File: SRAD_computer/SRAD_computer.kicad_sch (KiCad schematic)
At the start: 66 parts, among them J1 Terminal_3, J2 Conn_01x02, J3 UJ20-C-H-G-SMT-1-P16-TR, J4 Terminal_2, J5 Connector_3_Pol, J6 Micro_SD_Card, Q1 MMBT5551L, Q3 FDN340P, U1 NCP1117-3.3_SOT223, U2 W25Q128JVS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

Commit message: SD layout
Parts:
- added C18: 10u, TCLib:C_0805, symbol TCLib:C
- added R13: R, TCLib:R_0805, symbol TCLib:R
- added R14, R15: 10k, TCLib:R_0805, symbol TCLib:R
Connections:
- net +3V3: now also J6.4 (VDD), C18.1, R14.1, R15.1
- net GND: now also J6.6 (VSS), C18.2, R13.2
- net SD_CLK: now also U3.31 (GPIO20), R13.1; no longer U3.32 (GPIO21)
- net SD_CMD: now also U3.32 (GPIO21); no longer U3.34 (GPIO22)
- net SD_DAT1: now also U3.37 (GPIO25), R15.2; no longer U3.29 (GPIO18)
- net SD_DAT2: now also U3.35 (GPIO23), R14.2; no longer U3.37 (GPIO25)
- net SD_DAT3: now also U3.34 (GPIO22); no longer U3.35 (GPIO23)
- removed net SD_VSS: J6.6 (VSS), U3.31 (GPIO20)
- new net GPIO18: U3.29 (GPIO18)
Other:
- moved on the sheet: C10, C11, C12, C13, C14, C15, C16, C17, C6, C7, C8, C9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

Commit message: USB footprint changed & reboot sw added
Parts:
- removed J3: UJ20-C-H-G-SMT-1-P16-TR, my_lib:USB-C-samesky, symbol UJ20-C-H-G-SMT-1-P16-TR:UJ20-C-H-G-SMT-1-P16-TR
- added J7: UJ20-C-H-G-SMT-6-P16-TR, my_lib:SAMESKY_UJ20-C-H-G-SMT-6-P16-TR, symbol Rocketry_FC:UJ20-C-H-G-SMT-6-P16-TR
- added R16: 10k, TCLib:R_0805, symbol TCLib:R
- added S2: PTS810SJK250SMTR_LFS, PTS810SJK250SMTRLFS, symbol Rocketry_FC:PTS810SJK250SMTR_LFS
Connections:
- net +3V3: now also R16.1
- net GND: now also J7.A1 (GND), J7.A12 (GND__1), J7.B1 (GND__2), J7.B12 (GND__3), J7.SH1 (SHIELD), J7.SH2 (SHIELD__1), J7.SH3 (SHIELD__2), J7.SH4 (SHIELD__3), J7.SH5 (SHIELD__4), J7.SH6 (SHIELD__5), S2.3 (COM_1), S2.4 (COM_2)
- net RUN: now also R16.2, S2.1 (NO_1), S2.2 (NO_2)
- net USB_D+: now also J7.A6 (DP1), J7.B6 (DP2)
- net USB_D-: now also J7.A7 (DN1), J7.B7 (DN2)
- net VBUS: now also J7.A4 (VBUS), J7.A9 (VBUS__1), J7.B4 (VBUS__2), J7.B9 (VBUS__3)
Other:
- moved on the sheet: C2, C3, R12, R5, S1, Y1

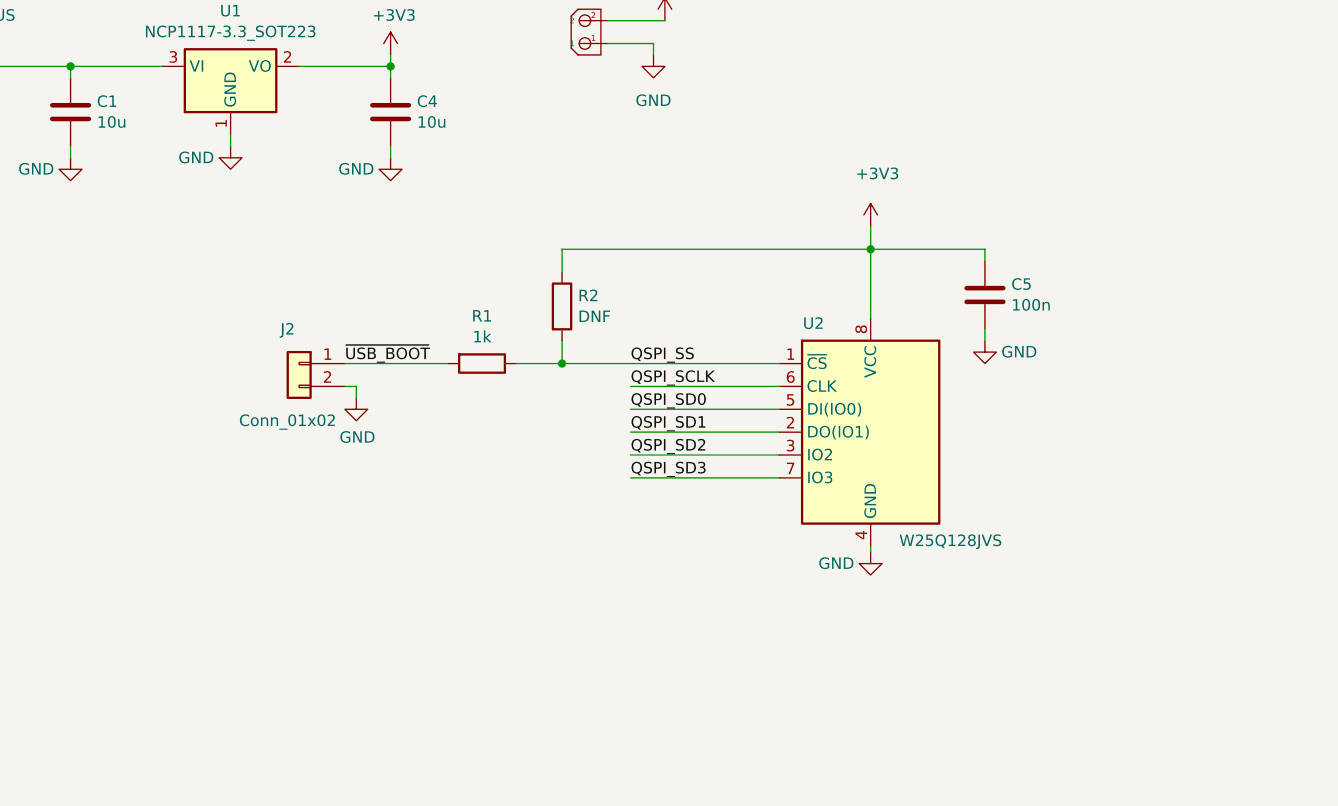
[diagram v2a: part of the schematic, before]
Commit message: reboot and bootsel buttons added
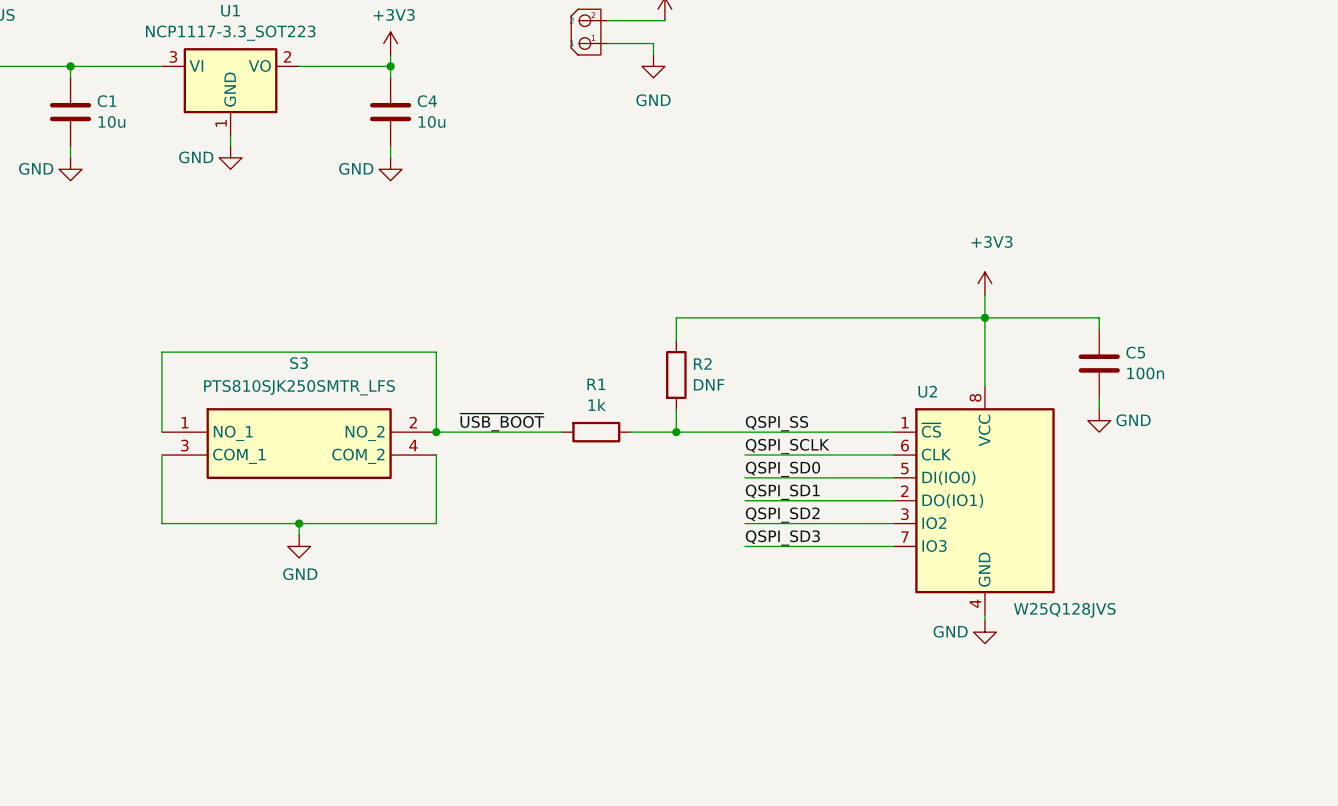
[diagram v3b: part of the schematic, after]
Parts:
- removed J2: Conn_01x02, Connector_PinHeader_2.54mm:PinHeader_1x02_P2.54mm_Vertical, symbol Connector_Generic:Conn_01x02
- added S3: PTS810SJK250SMTR_LFS, PTS810SJK250SMTRLFS, symbol Rocketry_FC:PTS810SJK250SMTR_LFS
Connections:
- net GND: now also S3.3 (COM_1), S3.4 (COM_2)
- net ~{USB_BOOT}: now also S3.1 (NO_1), S3.2 (NO_2)
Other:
- moved on the sheet: C5, R1, R2, U2

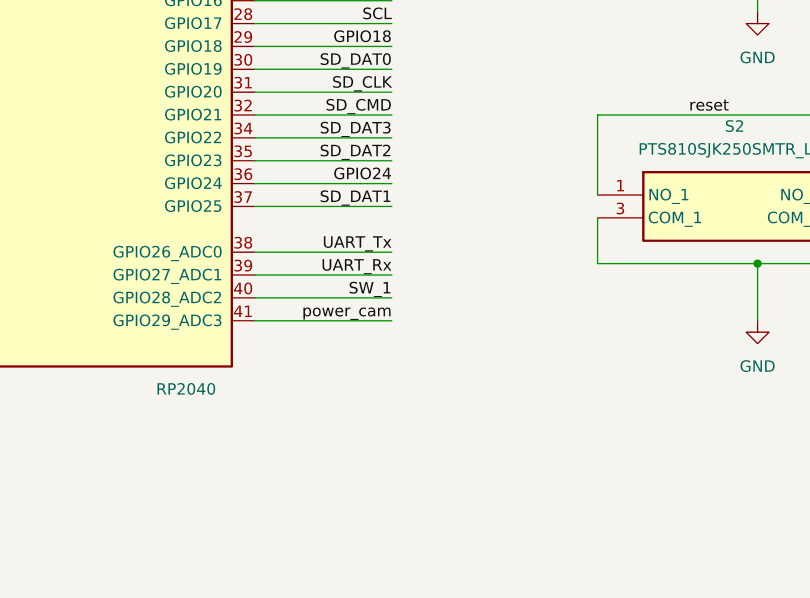
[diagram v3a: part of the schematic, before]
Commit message: Pin for battery level added
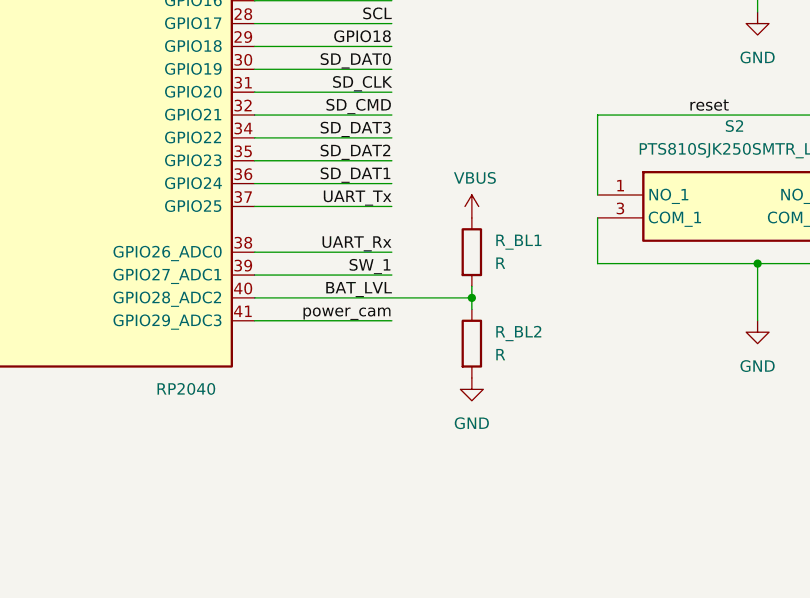
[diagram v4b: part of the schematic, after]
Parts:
- added R_BL1, R_BL2: R, TCLib:R_0805, symbol TCLib:R
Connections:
- net GPIO24 is gone; now on net SD_DAT1: U3.36 (GPIO24)
- net GND: now also R_BL2.2
- net SD_DAT1: no longer U3.37 (GPIO25)
- net SW_1: now also U3.39 (GPIO27_ADC1); no longer U3.40 (GPIO28_ADC2)
- net UART_Rx: now also U3.38 (GPIO26_ADC0); no longer U3.39 (GPIO27_ADC1)
- net UART_Tx: now also U3.37 (GPIO25); no longer U3.38 (GPIO26_ADC0)
- net VBUS: now also R_BL1.1
- new net BAT_LVL: R_BL1.2, R_BL2.1, U3.40 (GPIO28_ADC2)

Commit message: Gerber files added
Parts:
- removed J1: Terminal_3, TCLib:Bornera_3_P5mm, symbol TCLib:Terminal_3
- removed Q1: MMBT5551L, Package_TO_SOT_SMD:SOT-23, symbol Transistor_BJT:MMBT5551L
- removed Q3: FDN340P, Package_TO_SOT_SMD:SOT-23, symbol Transistor_FET:FDN340P
- removed R6, R7, R8: R, TCLib:R_0805, symbol Device:R
- added J1: Connector_2_Pol, TCLib:Molex_1x02_P2.54mm, symbol TCLib:Connector_2_Pol
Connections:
- net GND: now also J1.1
- net power_cam renamed servo
- net servo: now also J1.2
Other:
- note removed: "POWER CAM"

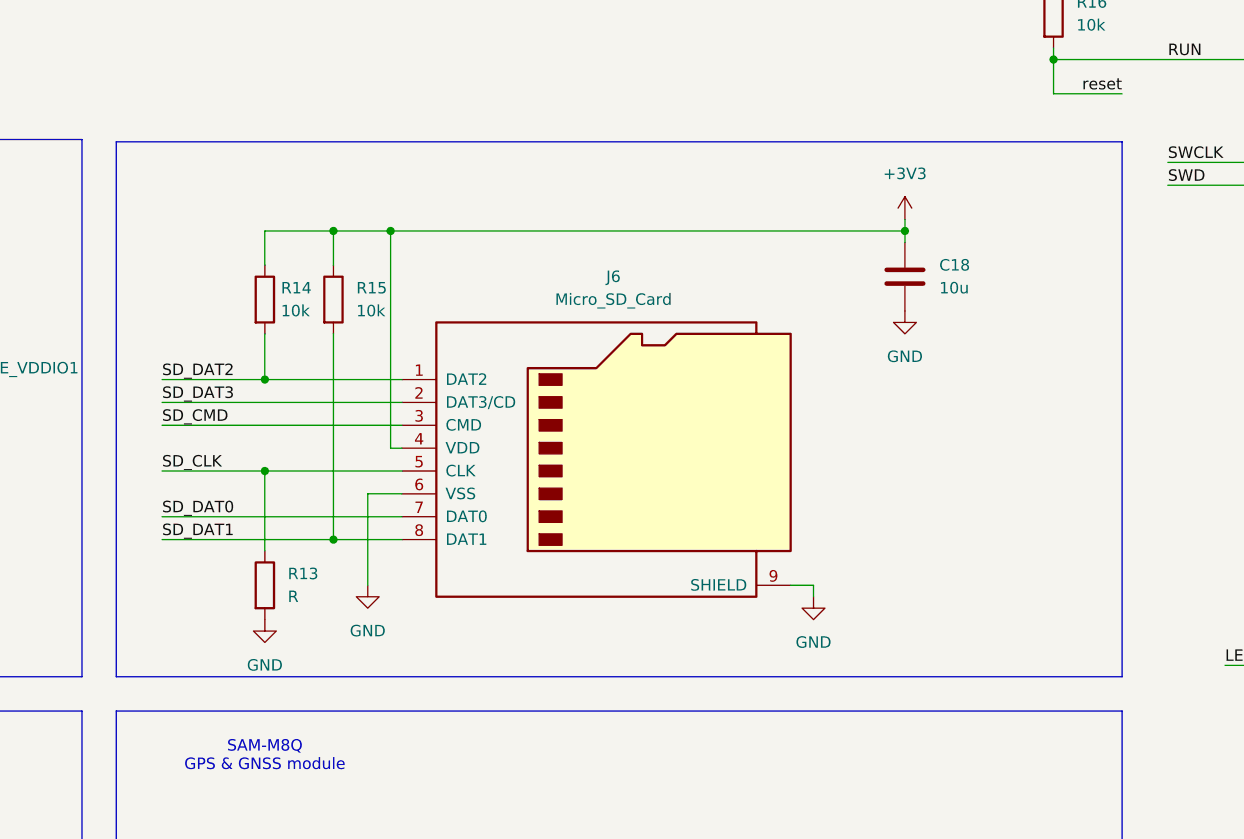
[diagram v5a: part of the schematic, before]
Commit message: changed SD socket & updated gerber files
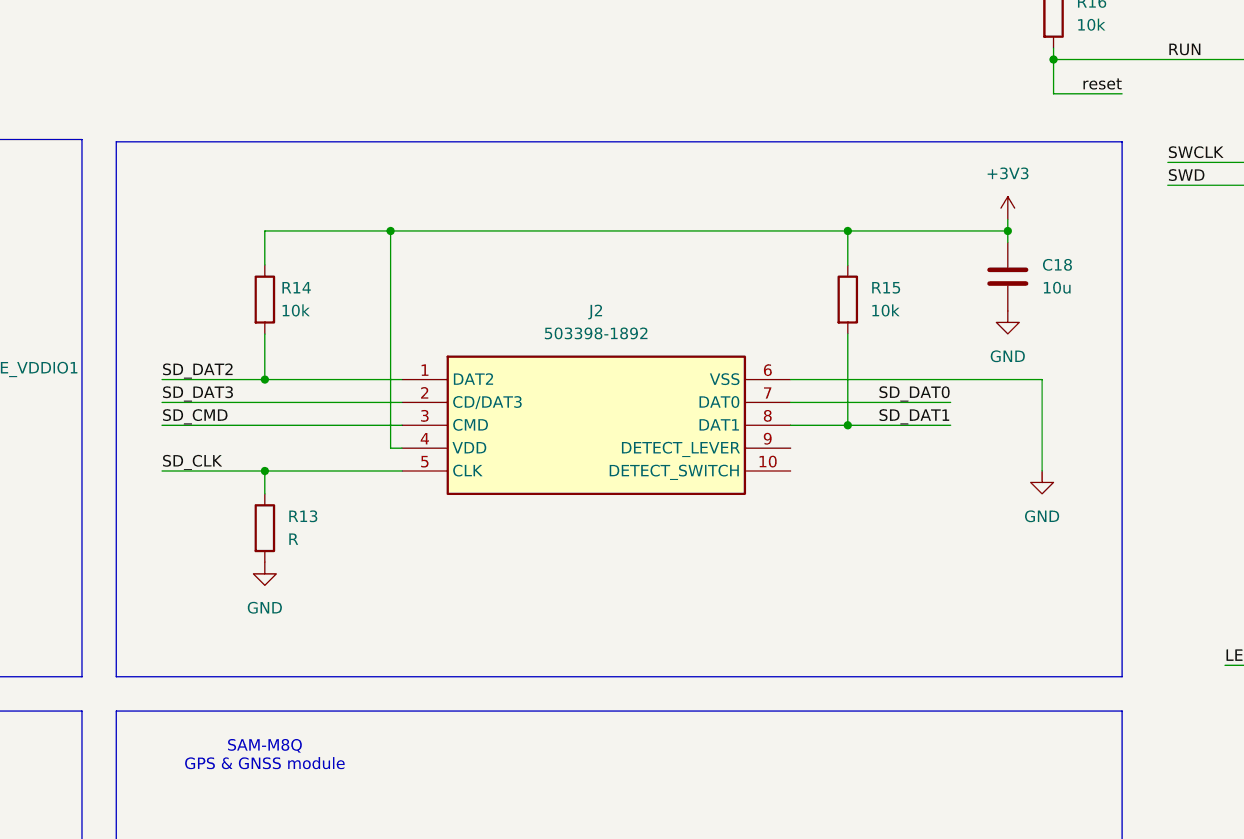
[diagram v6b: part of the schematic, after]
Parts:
- removed J6: Micro_SD_Card, my_lib:microSD_HC_Molex_47219-2001, symbol Connector:Micro_SD_Card
- added J2: 503398-1892, my_lib:503398-1892-1, symbol my_lib:503398-1892
- J1: footprint TCLib:Molex_1x02_P2.54mm -> TCLib:PinHeader_1x02_P2.54mm_Vertical
- J5: footprint TCLib:Molex_1x03_P2.54mm -> TCLib:PinHeader_1x03_P2.54mm_Vertical
- S1, S2, S3: footprint PTS810SJK250SMTRLFS -> my_lib:PTS810SJK250SMTRLFS
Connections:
- net +3V3: now also J2.4 (VDD)
- net GND: now also J2.6 (VSS)
- net SD_CLK: now also J2.5 (CLK)
- net SD_CMD: now also J2.3 (CMD)
- net SD_DAT0: now also J2.7 (DAT0)
- net SD_DAT1: now also J2.8 (DAT1)
- net SD_DAT2: now also J2.1 (DAT2)
- net SD_DAT3: now also J2.2 (CD/DAT3)
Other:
- moved on the sheet: C18, R13, R15
